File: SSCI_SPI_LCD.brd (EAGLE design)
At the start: 42 x 35 mm, 5 parts

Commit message: r0.1 prototype
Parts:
- added C1, C2: (no value), mylib:CR_1608
- added C3, C4, C5, C6, C7, C8, R1, R2, R3, R4, R5, R6: (no value), mylib:C0402
- added GIT1: (no value), git-revision:GIT-REVISION
- added IC1: (no value), mylib:SOT130P220X135-4N
- added IC2, IC5: (no value), mylib:SOT50P160X120-5N
- added IC3: 74LVC541_RGY, mylib:QFN50P460X360-20N
- added IC4: (no value), mylib:IC_08_1.27_150MIL
- added ICON1: r0.1, mylib:ICON_REVISION2.0
- added X1, X2: TSW-108-02-S-S, con-samtec.local:TSW-108-02-S-S
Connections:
- new net !CSR!: IC3.3, R2.2, X1.4, X2.4
- new net !CSR!-: IC2.1, IC3.17, IC4.1
- new net 3.3V: C2.1, C3.1, C4.1, C5.1, C6.1, C7.1, C8.1, IC1.3, IC2.5, IC3.20, IC4.3, IC4.7, IC4.8, IC5.5, LCD1.6, LCD1.7, R2.1
- new net 5V: C1.1, IC1.2, IC1.4, X1.1, X2.1
- new net CSL: IC3.7, R4.2, X1.7, X2.7
- new net CSL-: IC2.2, IC3.13, LCD1.3
- new net DISP: IC3.6, R3.2, X1.6, X2.6
- new net DISP-: IC3.14, LCD1.5
- new net GND: C1.2, C2.2, C3.2, C4.2, C5.2, C6.2, C7.2, C8.2, IC1.1, IC2.3, IC3.1, IC3.10, IC3.19, IC3.4, IC3.5, IC3.EP, IC4.4, IC5.3, LCD1.10, LCD1.8, LCD1.9, R1.1, R3.1, R4.1, R5.1, R6.1, X1.2, X2.2
- new net MISO: IC3.12, X1.5, X2.5
- new net MISO-: IC3.8, IC4.2, IC5.4, LCD1.2, R5.2
- new net MOSI: IC3.2, R1.2, X1.3, X2.3
- new net MOSI-: IC3.18, IC4.5, IC5.2
- new net N$2: IC2.4, IC5.1
- new net SCK: IC3.9, R6.2, X1.8, X2.8
- new net SCK-: IC3.11, IC4.6, LCD1.1
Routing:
- net MOSI: track 0.00 -> 54.0 mm
- net !CSR!: track 0.00 -> 51.0 mm
- net DISP: track 0.00 -> 50.5 mm
- net CSL: track 0.00 -> 50.0 mm
- net SCK: track 0.00 -> 48.0 mm
- net MISO: track 0.00 -> 46.7 mm, vias 0 -> 1
- net 5V: track 0.00 -> 46.0 mm
- net 3.3V: track 0.00 -> 30.1 mm, vias 0 -> 8
- net MISO-: track 0.00 -> 28.9 mm, vias 0 -> 3
- net SCK-: track 0.00 -> 24.3 mm, vias 0 -> 3
- net MOSI-: track 0.00 -> 21.2 mm, vias 0 -> 2
- net !CSR!-: track 0.00 -> 13.8 mm, vias 0 -> 2
- net CSL-: track 0.00 -> 11.5 mm, vias 0 -> 2
- net GND: track 0.00 -> 10.2 mm, vias 0 -> 10
- net DISP-: track 0.00 -> 8.84 mm
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- added copper zone on layer 16, net 3.3V
- added copper zone on layer 1, net GND
- added copper zone on layer 16, net GND

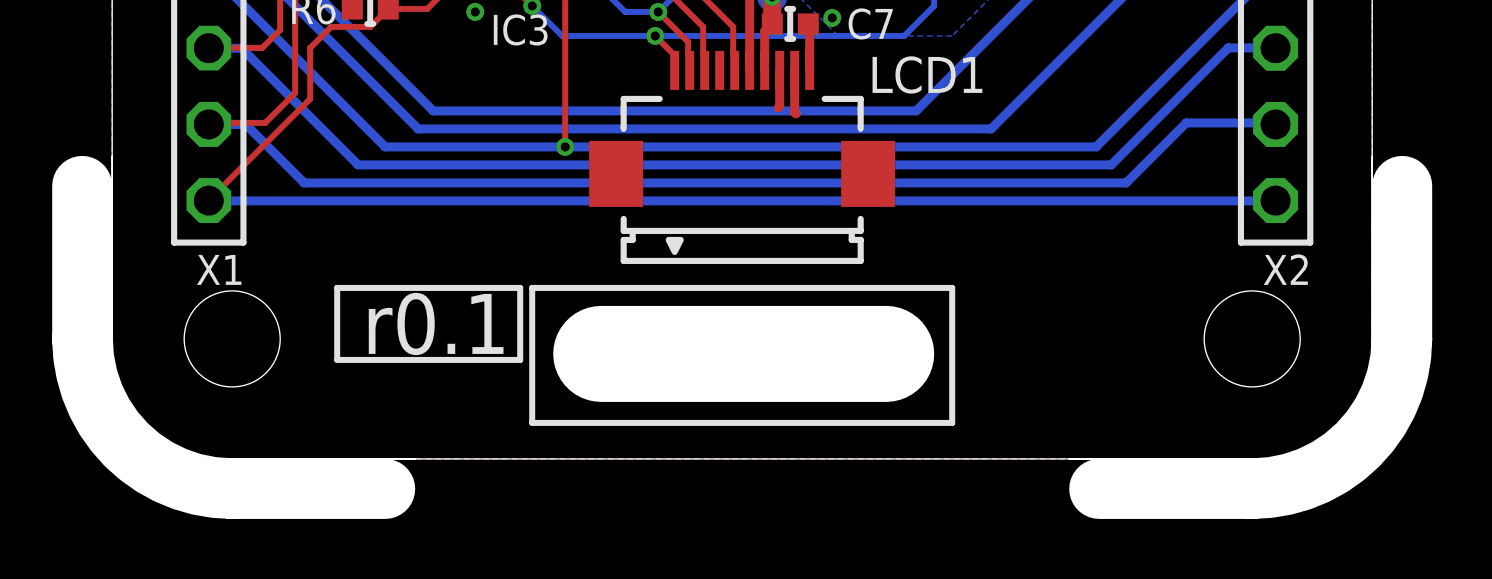
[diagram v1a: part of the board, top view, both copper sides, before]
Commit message: connectors silk
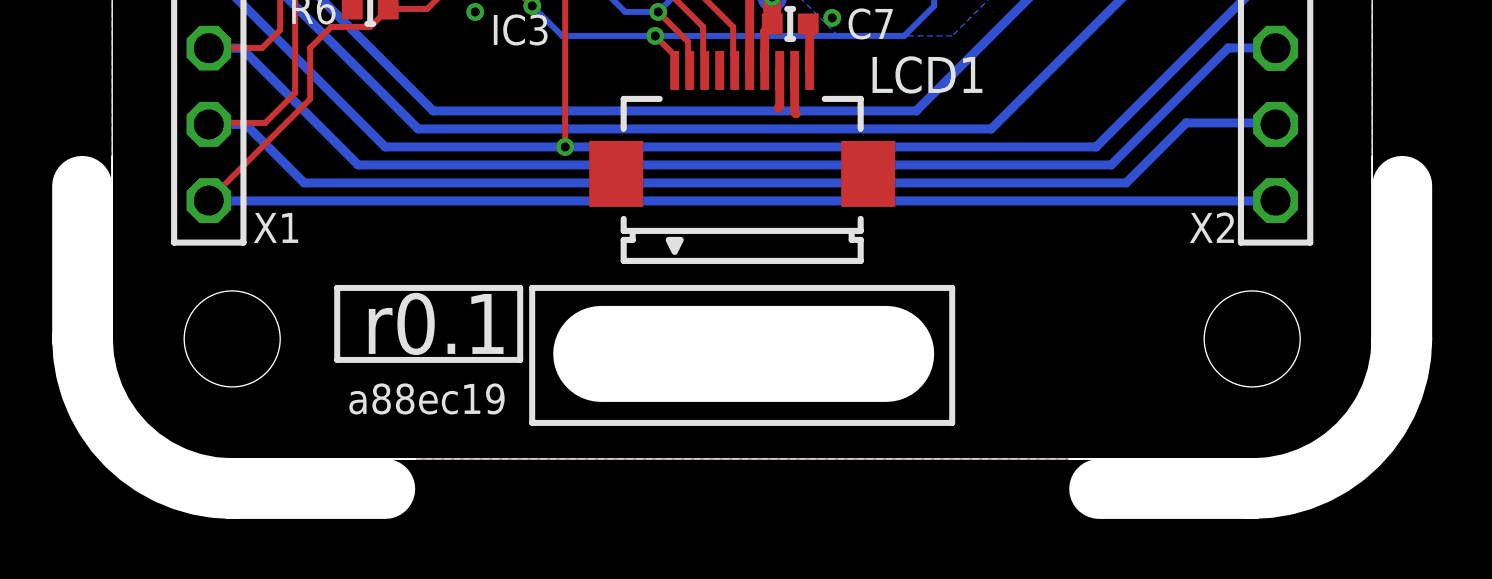
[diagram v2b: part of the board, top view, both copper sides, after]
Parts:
- GIT1: value (none) -> a88ec19
- moved GIT1 3.81 mm to (10.5, 2.00)
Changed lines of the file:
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@@
 <attribute name="NOT_COMPONENT" value="YES" x="4" y="4" size="1.778" layer="27" rot="R270" display="off"/>
 </element>
-<element name="GIT1" library="git-revision" package="GIT-REVISION" value="" x="7" y="0.5" smashed="yes">
-<attribute name="NOT_COMPONENT" value="YES" x="7" y="0.5" size="1.778" layer="27" display="off"/>
-<attribute name="VALUE" x="7" y="0.5" size="1" layer="21" ratio="20" align="center"/>
+<element name="GIT1" library="git-revision" package="GIT-REVISION" value="a88ec19" x="10.5" y="2">
+<attribute name="NOT_COMPONENT" value="YES" x="10.5" y="2" size="1.778" layer="27" display="off"/>
 </element>
 <element name="ICON1" library="mylib" package="ICON_REVISION2.0" value="r0.1" x="10.8" y="4.5" smashed="yes">
@@
 </element>
 <element name="X1" library="con-samtec.local" package="TSW-108-02-S-S" value="TSW-108-02-S-S" x="3.22" y="17.5006" locked="yes" smashed="yes" rot="R90">
-<attribute name="NAME" x="4.42" y="6.8006" size="1" layer="25" ratio="20" rot="R180"/>
+<attribute name="NAME" x="5.5" y="7.7" size="1" layer="25" ratio="20" rot="R180" align="center"/>
 <attribute name="VALUE" x="4.42" y="29.5006" size="1" layer="27" ratio="20" rot="R180"/>
 </element>
 <element name="X2" library="con-samtec.local" package="TSW-108-02-S-S" value="TSW-108-02-S-S" x="38.78" y="17.5" locked="yes" smashed="yes" rot="R90">
-<attribute name="NAME" x="39.98" y="6.8" size="1" layer="25" ratio="20" rot="R180"/>
+<attribute name="NAME" x="36.7" y="7.7" size="1" layer="25" ratio="20" align="center"/>
 <attribute name="VALUE" x="39.98" y="29.5" size="1" layer="27" ratio="20" rot="R180"/>
 </element>

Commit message: revision 0.1
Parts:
- added ICON2: (no value), mylib:ICON_OSHW
- GIT1: value a88ec19 -> 11642e8
- moved C2 14.1 mm to (19.2, 33.7)
- moved C1 14.1 mm to (19.2, 39.0)
- moved C3 14.1 mm to (29.5, 31.5)
- moved C4 14.1 mm to (22.8, 31.4)
- moved C6 14.1 mm to (29.5, 35.1)
- moved C7 14.1 mm to (32.6, 24.5)
- moved C8 14.1 mm to (32.6, 26.3)
- moved GIT1 14.1 mm to (20.5, 12.0)
- moved IC1 14.1 mm to (19.1, 36.4)
- moved IC2 14.1 mm to (29.5, 29.7)
- moved IC3 14.1 mm to (22.8, 28.0)
- moved IC4 14.1 mm to (37.0, 32.0)
- moved ICON1 14.1 mm to (20.8, 14.5)
- moved LCD1 14.1 mm to (31.0, 19.5)
- moved P1 14.1 mm to (48.0, 14.0)
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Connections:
- net GND: now also LCD1.PAD1, LCD1.PAD2
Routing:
- net GND: track 10.2 -> 22.6 mm, vias 10 -> 12
- net SCK-: track 24.3 -> 22.7 mm
- net !CSR!-: track 13.8 -> 14.9 mm
- net MOSI-: track 21.2 -> 22.0 mm
- net 3.3V: track 30.1 -> 30.0 mm, vias 8 -> 9
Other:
- board size 42 x 35 mm -> 114 x 100 mm
- board text added: "@_K4ZUKI_"
